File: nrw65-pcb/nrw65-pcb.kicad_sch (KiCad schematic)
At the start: 122 parts, among them U1 nice_nano

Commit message: Work in progress
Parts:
- added BT1: Battery_Cell, Connector_JST:JST_PH_S2B-PH-K_1x02_P2.00mm_Horizontal, symbol Device:Battery_Cell
- added SW1: SW_DIP_x01, Kicad footprints:MSK-12C02, symbol Switch:SW_DIP_x01
- added SW2: SW_DIP_x01, Connector_Wire:SolderWire-0.75sqmm_1x02_P7mm_D1.25mm_OD3.5mm, symbol Switch:SW_DIP_x01
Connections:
- net bat: now reaches U1.13 (BAT+)
- net bat: now also U1.29 (BAT+), SW1.2
- net gnd: now reaches U1.14 (GND)
- net gnd: now also U1.3 (GND), U1.4 (GND), BT1.2 (-), SW2.1
- net rst: now reaches U1.15 (RST)
- net rst: now also SW2.2
- new net: BT1.1 (+), SW1.1
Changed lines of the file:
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@@
   (junction (at 151.13 135.89) (diameter 0) (color 0 0 0 0)
   )
+  (junction (at 250.19 40.64) (diameter 0) (color 0 0 0 0)
+  )
   (junction (at 54.61 97.79) (diameter 0) (color 0 0 0 0)
   )
@@
   (junction (at 100.33 57.15) (diameter 0) (color 0 0 0 0)
   )
+  (junction (at 212.09 48.26) (diameter 0) (color 0 0 0 0)
+  )
   (junction (at 43.18 57.15) (diameter 0) (color 0 0 0 0)
   )
@@
     (stroke (width 0) (type default))
   )
+  (wire (pts (xy 195.58 99.06) (xy 195.58 105.41))
+    (stroke (width 0) (type default))
+  )
   (wire (pts (xy 151.13 49.53) (xy 162.56 49.53))
     (stroke (width 0) (type default))
@@
     (stroke (width 0) (type default))
   )
+  (wire (pts (xy 209.55 48.26) (xy 212.09 48.26))
+    (stroke (width 0) (type default))
+  )
   (wire (pts (xy 59.69 49.53) (xy 71.12 49.53))
     (stroke (width 0) (type default))
@@
     (stroke (width 0) (type default))
   )
+  (wire (pts (xy 250.19 38.1) (xy 250.19 40.64))
+    (stroke (width 0) (type default))
+  )
   (wire (pts (xy 105.41 69.85) (xy 116.84 69.85))
     (stroke (width 0) (type default))
@@
     (stroke (width 0) (type default))
   )
+  (wire (pts (xy 250.19 40.64) (xy 252.73 40.64))
+    (stroke (width 0) (type default))
+  )
   (wire (pts (xy 36.83 130.81) (xy 48.26 130.81))
     (stroke (width 0) (type default))
@@
     (stroke (width 0) (type default))
   )
+  (wire (pts (xy 212.09 45.72) (xy 212.09 48.26))
+    (stroke (width 0) (type default))
+  )
   (wire (pts (xy 43.18 57.15) (xy 43.18 77.47))
     (stroke (width 0) (type default))
@@
     (stroke (width 0) (type default))
   )
+  (global_label "rst" (shape input) (at 243.84 99.06 0) (fields_autoplaced)
+    (effects (font (size 1.27 1.27)) (justify left))
+    (property "Intersheetrefs" "${INTERSHEET_REFS}" (at 249.3652 99.06 0)
+      (effects (font (size 1.27 1.27)) (justify left) hide)
+    )
+  )
+  (global_label "gnd" (shape input) (at 228.6 99.06 180) (fields_autoplaced)
+    (effects (font (size 1.27 1.27)) (justify right))
+    (property "Intersheetrefs" "${INTERSHEET_REFS}" (at 222.1678 99.06 0)
+      (effects (font (size 1.27 1.27)) (justify right) hide)
+    )
+  )
+  (global_label "gnd" (shape input) (at 250.19 43.18 0) (fields_autoplaced)
+    (effects (font (size 1.27 1.27)) (justify left))
+    (property "Intersheetrefs" "${INTERSHEET_REFS}" (at 256.6222 43.18 0)
+      (effects (font (size 1.27 1.27)) (justify left) hide)
+    )
+  )
+  (global_label "gnd" (shape input) (at 209.55 48.26 180) (fields_autoplaced)
+    (effects (font (size 1.27 1.27)) (justify right))
+    (property "Intersheetrefs" "${INTERSHEET_REFS}" (at 203.1178 48.26 0)
+      (effects (font (size 1.27 1.27)) (justify right) hide)
+    )
+  )
+  (global_label "bat" (shape input) (at 252.73 40.64 0) (fields_autoplaced)
+    (effects (font (size 1.27 1.27)) (justify left))
+    (property "Intersheetrefs" "${INTERSHEET_REFS}" (at 258.7389 40.64 0)
+      (effects (font (size 1.27 1.27)) (justify left) hide)
+    )
+  )
+  (global_label "bat" (shape input) (at 210.82 99.06 0) (fields_autoplaced)
+    (effects (font (size 1.27 1.27)) (justify left))
+    (property "Intersheetrefs" "${INTERSHEET_REFS}" (at 216.8289 99.06 0)
+      (effects (font (size 1.27 1.27)) (justify left) hide)
+    )
+  )
+  (global_label "rst" (shape input) (at 250.19 45.72 0) (fields_autoplaced)
+    (effects (font (size 1.27 1.27)) (justify left))
+    (property "Intersheetrefs" "${INTERSHEET_REFS}" (at 255.7152 45.72 0)
+      (effects (font (size 1.27 1.27)) (justify left) hide)
+    )
+  )
+  (global_label "gnd" (shape input) (at 195.58 113.03 180) (fields_autoplaced)
+    (effects (font (size 1.27 1.27)) (justify right))
+    (property "Intersheetrefs" "${INTERSHEET_REFS}" (at 189.1478 113.03 0)
+      (effects (font (size 1.27 1.27)) (justify right) hide)
+    )
+  )
   (symbol (lib_id "PCM_marbastlib-mx:MX_SW_HS") (at 160.02 105.41 0) (unit 1)
     (in_bom yes) (on_board yes) (dnp no) (fields_autoplaced)
@@
     )
   )
+  (symbol (lib_id "Switch:SW_DIP_x01") (at 236.22 99.06 0) (unit 1)
+    (in_bom yes) (on_board yes) (dnp no) (fields_autoplaced)
+    (property "Reference" "SW2" (at 236.22 91.44 0)
+      (effects (font (size 1.27 1.27)))
+    )
+    (property "Value" "SW_DIP_x01" (at 236.22 93.98 0)
+      (effects (font (size 1.27 1.27)))
+    )
+    (property "Footprint" "Connector_Wire:SolderWire-0.75sqmm_1x02_P7mm_D1.25mm_OD3.5mm" (at 236.22 99.06 0)
+      (effects (font (size 1.27 1.27)) hide)
+    )
+    (property "Datasheet" "~" (at 236.22 99.06 0)
+      (effects (font (size 1.27 1.27)) hide)
+    )
+    (pin "1")
+    (pin "2")
+    (instances
+      (project "nrw65-pcb"
+        (path "/4c9b8cf1-f4cc-44ac-a61e-1dc7db89f0ef"
+          (reference "SW2") (unit 1)
+        )
+      )
+    )
+  )
   (symbol (lib_id "PCM_marbastlib-mx:MX_SW_HS") (at 34.29 59.69 0) (unit 1)
     (in_bom yes) (on_board yes) (dnp no) (fields_autoplaced)
@@
     )
   )
+  (symbol (lib_id "Switch:SW_DIP_x01") (at 203.2 99.06 0) (unit 1)
+    (in_bom yes) (on_board yes) (dnp no) (fields_autoplaced)
+    (property "Reference" "SW1" (at 203.2 91.44 0)
+      (effects (font (size 1.27 1.27)))
+    )
+    (property "Value" "SW_DIP_x01" (at 203.2 93.98 0)
+      (effects (font (size 1.27 1.27)))
+    )
+    (property "Footprint" "Kicad footprints:MSK-12C02" (at 203.2 99.06 0)
+      (effects (font (size 1.27 1.27)) hide)
+    )
+    (property "Datasheet" "~" (at 203.2 99.06 0)
+      (effects (font (size 1.27 1.27)) hide)
+    )
+    (pin "1")
+    (pin "2")
+    (instances
+      (project "nrw65-pcb"
+        (path "/4c9b8cf1-f4cc-44ac-a61e-1dc7db89f0ef"
+          (reference "SW1") (unit 1)
+        )
+      )
+    )
+  )
   (symbol (lib_id "PCM_marbastlib-mx:MX_stab") (at 38.1 148.59 0) (unit 1)
     (in_bom yes) (on_board yes) (dnp no) (fields_autoplaced)
@@
         )
       )
+    )
+  )
+  (symbol (lib_id "Device:Battery_Cell") (at 195.58 110.49 0) (unit 1)
+    (in_bom yes) (on_board yes) (dnp no) (fields_autoplaced)
+    (property "Reference" "BT1" (at 199.39 107.3785 0)
+      (effects (font (size 1.27 1.27)) (justify left))
+    )
+    (property "Value" "Battery_Cell" (at 199.39 109.9185 0)
+      (effects (font (size 1.27 1.27)) (justify left))
+    )
+    (property "Footprint" "Connector_JST:JST_PH_S2B-PH-K_1x02_P2.00mm_Horizontal" (at 195.58 108.966 90)
+      (effects (font (size 1.27 1.27)) hide)
+    )
+    (property "Datasheet" "~" (at 195.58 108.966 90)
+      (effects (font (size 1.27 1.27)) hide)
+    )
+    (pin "1")
+    (pin "2")
+    (instances
+      (project "nrw65-pcb"
+        (path "/4c9b8cf1-f4cc-44ac-a61e-1dc7db89f0ef"
+          (reference "BT1") (unit 1)
+        )
+      )

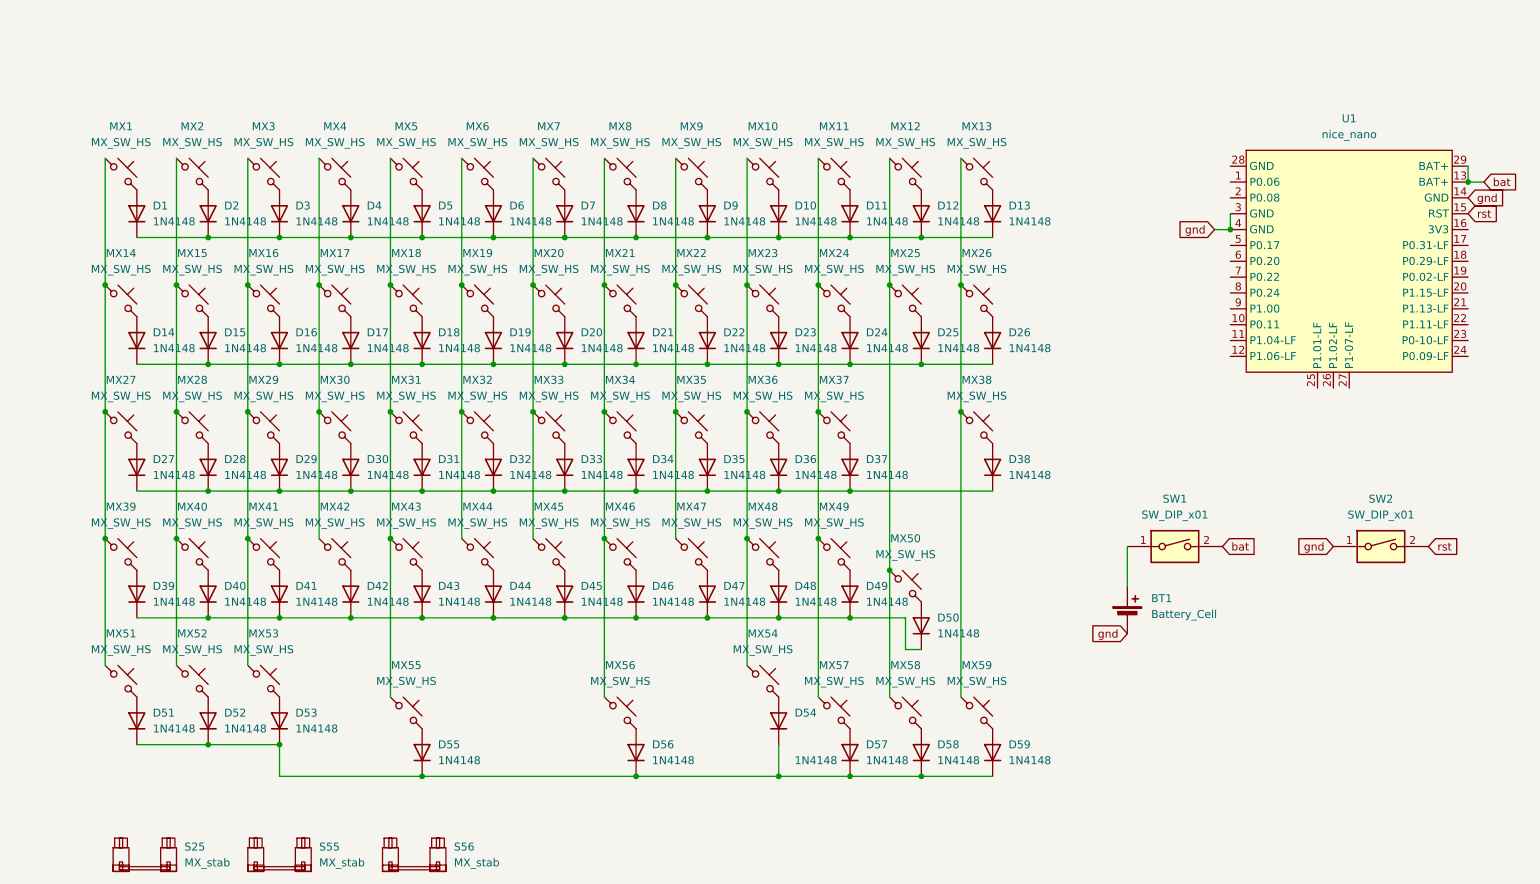
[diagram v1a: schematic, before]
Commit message: add pcb and rcheme routing
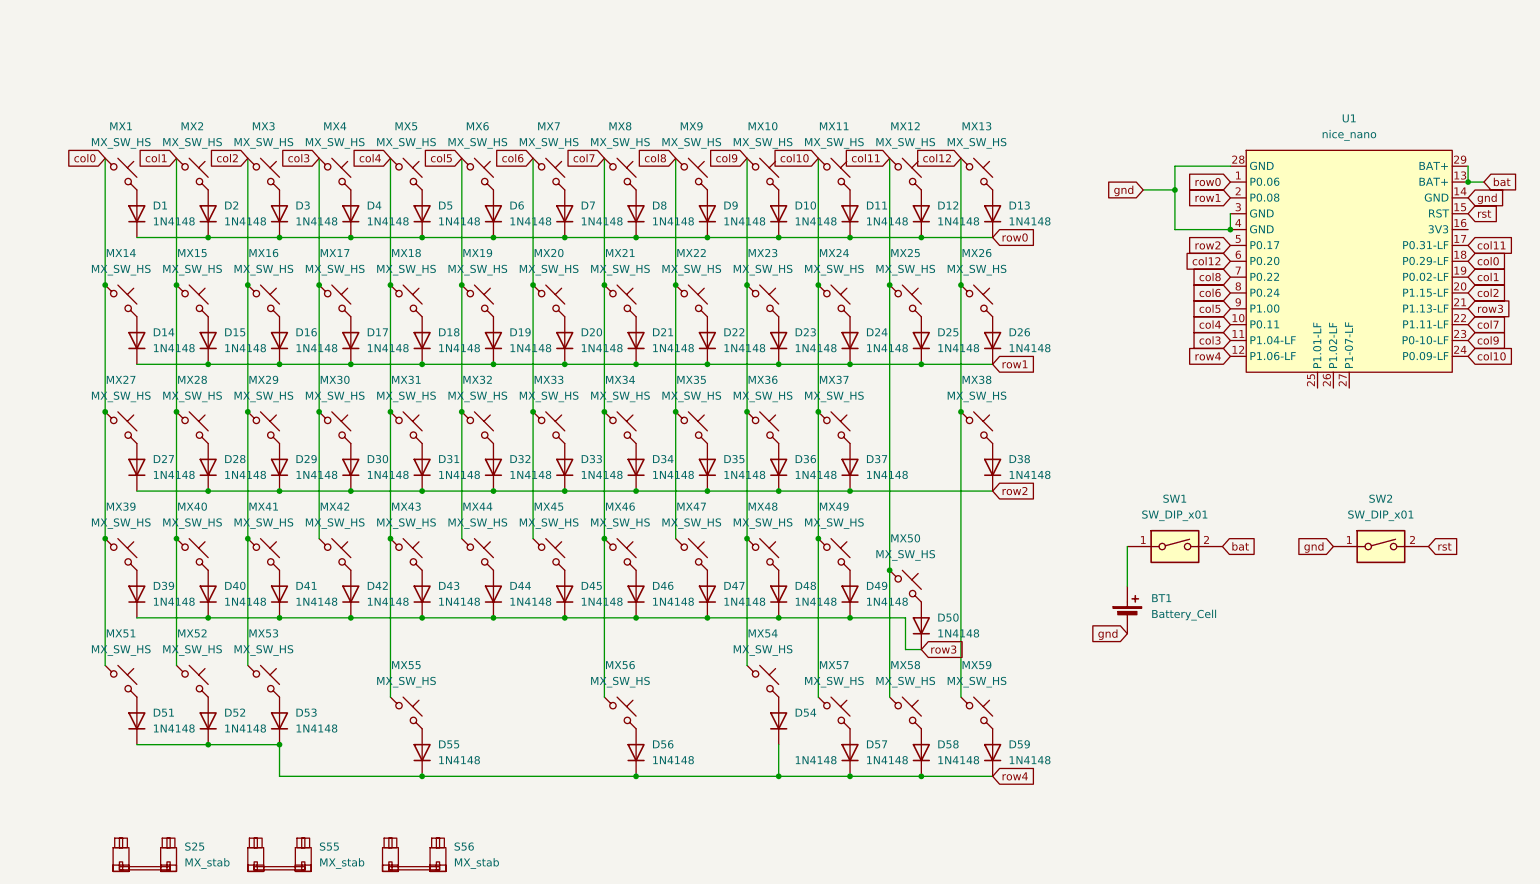
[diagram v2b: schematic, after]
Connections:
- net gnd: now also U1.28 (GND)
- net col11: now reaches MX12.1, MX25.1, MX50.1, MX58.1
- net col11: now also U1.17 (P0.31-LF)
- net col0: now reaches MX1.1, MX14.1, MX27.1, MX39.1, MX51.1
- net col0: now also U1.18 (P0.29-LF)
- net col12: now reaches MX13.1, MX26.1, MX38.1, MX59.1
- net col12: now also U1.6 (P0.20)
- net row3: now reaches D39.1 (K), D40.1 (K), D41.1 (K), D42.1 (K), D43.1 (K), D44.1 (K), D45.1 (K), D46.1 (K), D47.1 (K), D48.1 (K), D49.1 (K), D50.1 (K)
- net row3: now also U1.21 (P1.13-LF)
- net row2: now reaches D27.1 (K), D28.1 (K), D29.1 (K), D30.1 (K), D31.1 (K), D32.1 (K), D33.1 (K), D34.1 (K), D35.1 (K), D36.1 (K), D37.1 (K), D38.1 (K)
- net row2: now also U1.5 (P0.17)
- net col2: now reaches MX16.1, MX29.1, MX3.1, MX41.1, MX53.1
- net col2: now also U1.20 (P1.15-LF)
- net col8: now reaches MX22.1, MX35.1, MX47.1, MX9.1
- net col8: now also U1.7 (P0.22)
- net row0: now reaches D1.1 (K), D10.1 (K), D11.1 (K), D12.1 (K), D13.1 (K), D2.1 (K), D3.1 (K), D4.1 (K), D5.1 (K), D6.1 (K), D7.1 (K), D8.1 (K), D9.1 (K)
- net row0: now also U1.1 (P0.06)
- net col5: now reaches MX19.1, MX32.1, MX44.1, MX6.1
- net col5: now also U1.9 (P1.00)
- net row1: now reaches D14.1 (K), D15.1 (K), D16.1 (K), D17.1 (K), D18.1 (K), D19.1 (K), D20.1 (K), D21.1 (K), D22.1 (K), D23.1 (K), D24.1 (K), D25.1 (K), D26.1 (K)
- net row1: now also U1.2 (P0.08)
- net col9: now reaches MX10.1, MX23.1, MX36.1, MX48.1, MX54.1
- net col9: now also U1.23 (P0-10-LF)
- net col10: now reaches MX11.1, MX24.1, MX37.1, MX49.1, MX57.1
- net col10: now also U1.24 (P0.09-LF)
- net col4: now reaches MX18.1, MX31.1, MX43.1, MX5.1, MX55.1
- net col4: now also U1.10 (P0.11)
- net row4: now reaches D51.1 (K), D52.1 (K), D53.1 (K), D54.1 (K), D55.1 (K), D56.1 (K), D57.1 (K), D58.1 (K), D59.1 (K)
- net row4: now also U1.12 (P1.06-LF)
- net col3: now reaches U1.11 (P1.04-LF)
- net col3: now also MX17.1, MX30.1, MX4.1, MX42.1
- net col1: now reaches U1.19 (P0.02-LF)
- net col1: now also MX15.1, MX2.1, MX28.1, MX40.1, MX52.1
- net col7: now reaches U1.22 (P1.11-LF)
- net col7: now also MX21.1, MX34.1, MX46.1, MX56.1, MX8.1
- net col6: now reaches U1.8 (P0.24)
- net col6: now also MX20.1, MX33.1, MX45.1, MX7.1

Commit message: Work in progress: change to Pro Micro footprint, add rotary encoder, change to MX+KS33 hot swap footprints, reroute tracks.
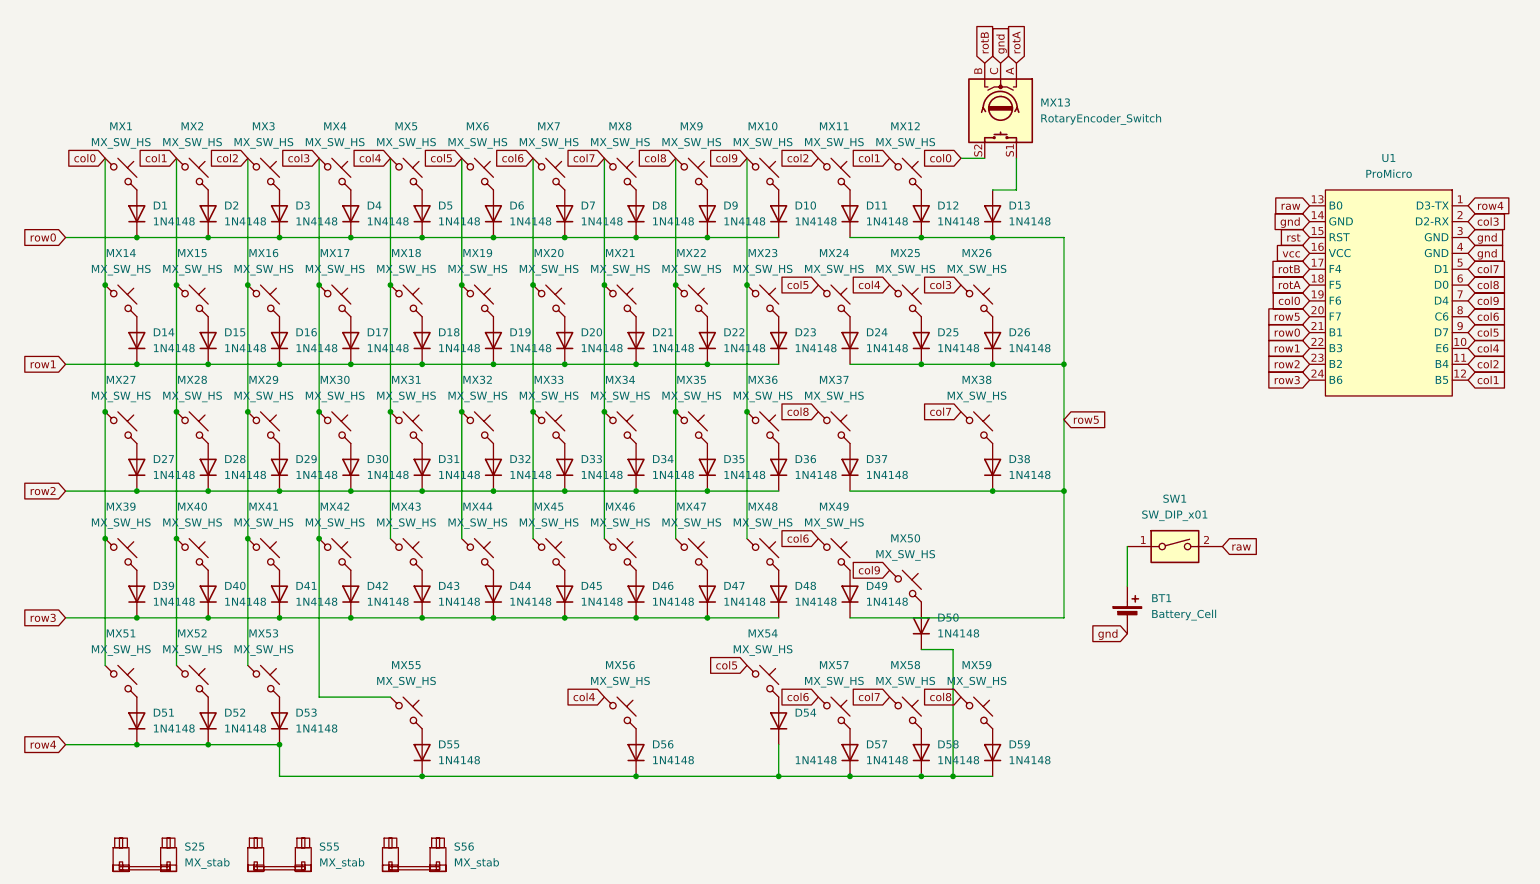
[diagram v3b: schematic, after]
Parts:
- removed MX13: MX_SW_HS, PCM_marbastlib-mx:SW_MX_HS_S_1u_REVERSE, symbol PCM_marbastlib-mx:MX_SW_HS
- removed SW2: SW_DIP_x01, Connector_Wire:SolderWire-0.75sqmm_1x02_P7mm_D1.25mm_OD3.5mm, symbol Switch:SW_DIP_x01
- removed U1: nice_nano, PCM_marbastlib-xp-promicroish:nice_nano_AH_USBup, symbol PCM_marbastlib-promicroish:nice_nano
- added MX13: RotaryEncoder_Switch, PCM_marbastlib-various:ROT_Alps_EC11E-Switch_Invisible_designator, symbol Device:RotaryEncoder_Switch
- added U1: ProMicro, PCM_marbastlib-xp-promicroish:ProMicro_USBup, symbol PCM_marbastlib-promicroish:Arduino_ProMicro
- MX1, MX10, MX11, MX14, MX15, MX16, MX17, MX18, MX19, MX2, MX20, MX21, MX22, MX23, MX24, MX25, MX26, MX28, MX29, MX3, MX30, MX31, MX32, MX33, MX34, MX35, MX36, MX37, MX38, MX4, MX40, MX41, MX42, MX43, MX44, MX45, MX46, MX47, MX48, MX49, MX5, MX50, MX55, MX56, MX57, MX58, MX59, MX6, MX7, MX8, MX9: footprint PCM_marbastlib-mx:SW_MX_HS_S_1u_REVERSE -> PCM_marbastlib-mx:SW_MX_HS_S_1u_REVERSE+KS33_HS
- MX12: footprint PCM_marbastlib-mx:SW_MX_HS_S_1u_REVERSE -> PCM_marbastlib-mx:SW_MX_1u+KS33
- MX27, MX51, MX52, MX53, MX54: footprint PCM_marbastlib-mx:SW_MX_HS_S_1.25u_REVERSE -> PCM_marbastlib-mx:SW_MX_HS_S_1.25u_REVERSE+KS33_HS
- MX39: footprint PCM_marbastlib-mx:SW_MX_HS_S_1.5u_REVERSE -> PCM_marbastlib-mx:SW_MX_HS_S_1.5u_REVERSE+KS33_HS
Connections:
- net col0: now also MX13.S2, U1.19 (F6)
- net col1: now also MX12.1, U1.12 (B5)
- net col2: now also MX11.1, U1.11 (B4)
- net col3: now also MX26.1, MX55.1, U1.2 (D2-RX)
- net col4: now also MX25.1, MX56.1, U1.10 (E6); no longer MX55.1
- net col5: now also MX24.1, MX54.1, U1.9 (D7)
- net col6: now also MX49.1, MX57.1, U1.8 (C6)
- net col7: now also MX38.1, MX58.1, U1.5 (D1); no longer MX56.1
- net col8: now also MX37.1, MX59.1, U1.6 (D0)
- net col9: now also MX50.1, U1.7 (D4); no longer MX54.1
- net gnd: now also MX13.C, U1.14 (GND), U1.3 (GND), U1.4 (GND)
- net row0: now also U1.21 (B1); no longer D11.1 (K), D12.1 (K), D13.1 (K)
- net row1: now also U1.22 (B3); no longer D24.1 (K), D25.1 (K), D26.1 (K)
- net row2: now also U1.23 (B2); no longer D37.1 (K), D38.1 (K)
- net row3: now also U1.24 (B6); no longer D49.1 (K), D50.1 (K)
- net row4: now also D50.1 (K), U1.1 (D3-TX)
- net rst: now also U1.15 (RST)
- net at D13.2 (A): now also MX13.S1
- net bat renamed raw
- net raw: now also U1.13 (B0)
- removed net col10: MX11.1, MX24.1, MX37.1, MX49.1, MX57.1
- removed net col11: MX12.1, MX25.1, MX50.1, MX58.1
- removed net col12: MX26.1, MX38.1, MX59.1
- new net rotA: MX13.A, U1.18 (F5)
- new net rotB: MX13.B, U1.17 (F4)
- new net row5: D11.1 (K), D12.1 (K), D13.1 (K), D24.1 (K), D25.1 (K), D26.1 (K), D37.1 (K), D38.1 (K), D49.1 (K), U1.20 (F7)
- new net vcc: U1.16 (VCC)
